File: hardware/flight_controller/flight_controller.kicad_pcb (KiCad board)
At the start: 2 copper layers, 156.2 x 48.3 mm, 14 parts, among them J1 Conn_02x04_Odd_Even, J2 Conn_01x03, J3 Conn_01x03, J4 Conn_01x03, J5 Conn_01x03, J6 Conn_01x05, J7 Conn_01x03, U1 Teensy3.6, U2 Logic_Level_Converter, U3 Logic_Level_Converter

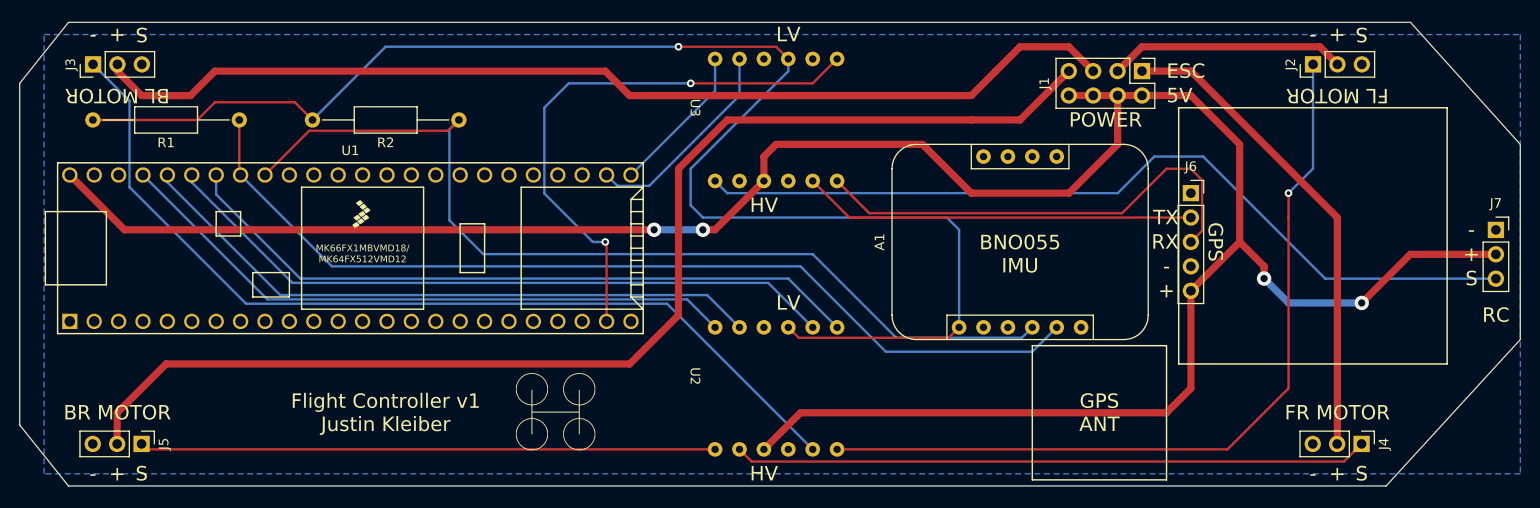
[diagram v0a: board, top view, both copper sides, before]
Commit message: Updates FC board to v1.1 due to footprint size error
Need to choose different parts and include BOM for hardware
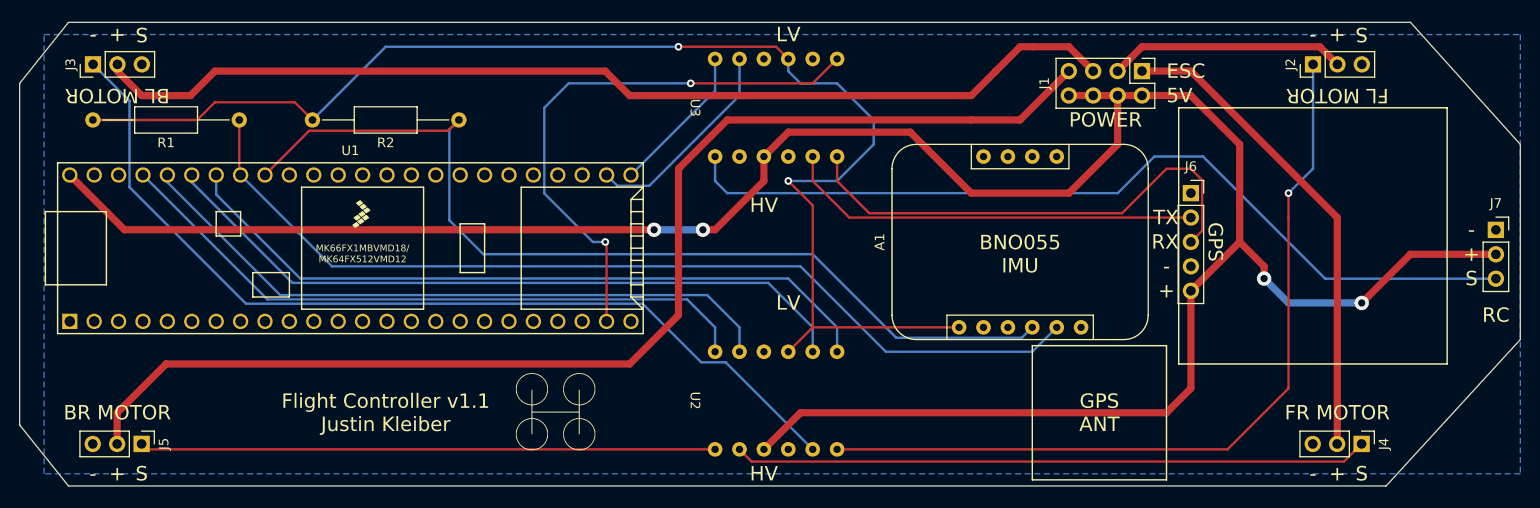
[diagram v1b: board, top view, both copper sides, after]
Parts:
- moved U2 2.54 mm to (171.4, 123.2)
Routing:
- net 3.3V: track 154.9 -> 138.0 mm, vias 1 -> 2
- net A9: track 66.1 -> 68.7 mm
- net A8: track 66.6 -> 69.1 mm
- net A6: track 72.4 -> 74.9 mm
- net iA6b_motors: track 88.7 -> 91.2 mm
- net GPS_TX: track 40.9 -> 43.5 mm
- net GPS_RX: track 48.7 -> 51.3 mm
- net A7: track 71.6 -> 74.2 mm
- net 5V_VIN: track 252.5 -> 253.6 mm
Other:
- board text added: "Flight Controller v1.1 Justin Kleiber"
- board text removed: "Flight Controller v1 Justin Kleiber"
